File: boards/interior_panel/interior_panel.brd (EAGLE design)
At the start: 99.1 x 71.1 mm, 27 parts, among them IC1 LM2576, IC2 DS1307, J1 POWER_JACKPTH_BREAD, Q1 MOSFET-NCHANNELFQP30N06L, U1 ATMEGA328P, U2 EXT ENCLOSURE, U3 DISPLAY, Y1 16MHz, Y2 32.786kHz

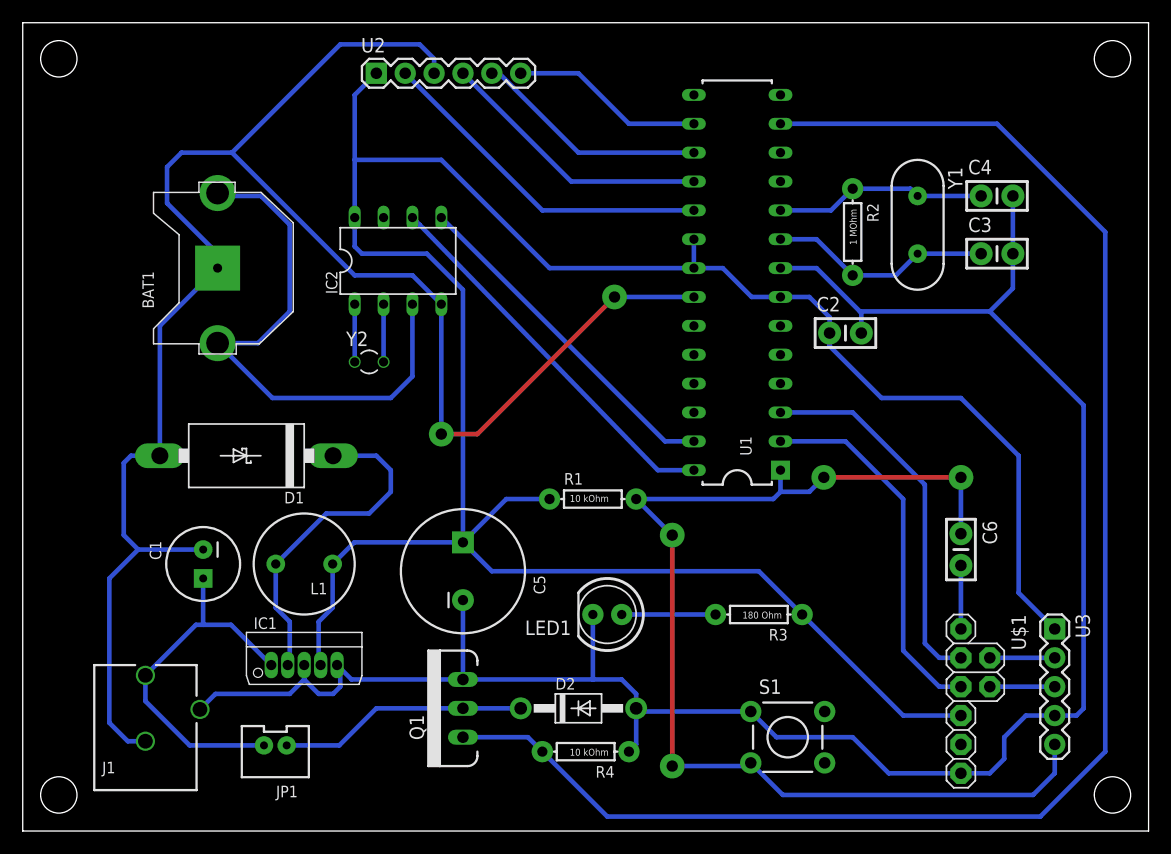
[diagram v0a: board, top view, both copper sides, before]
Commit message: Interior open command added
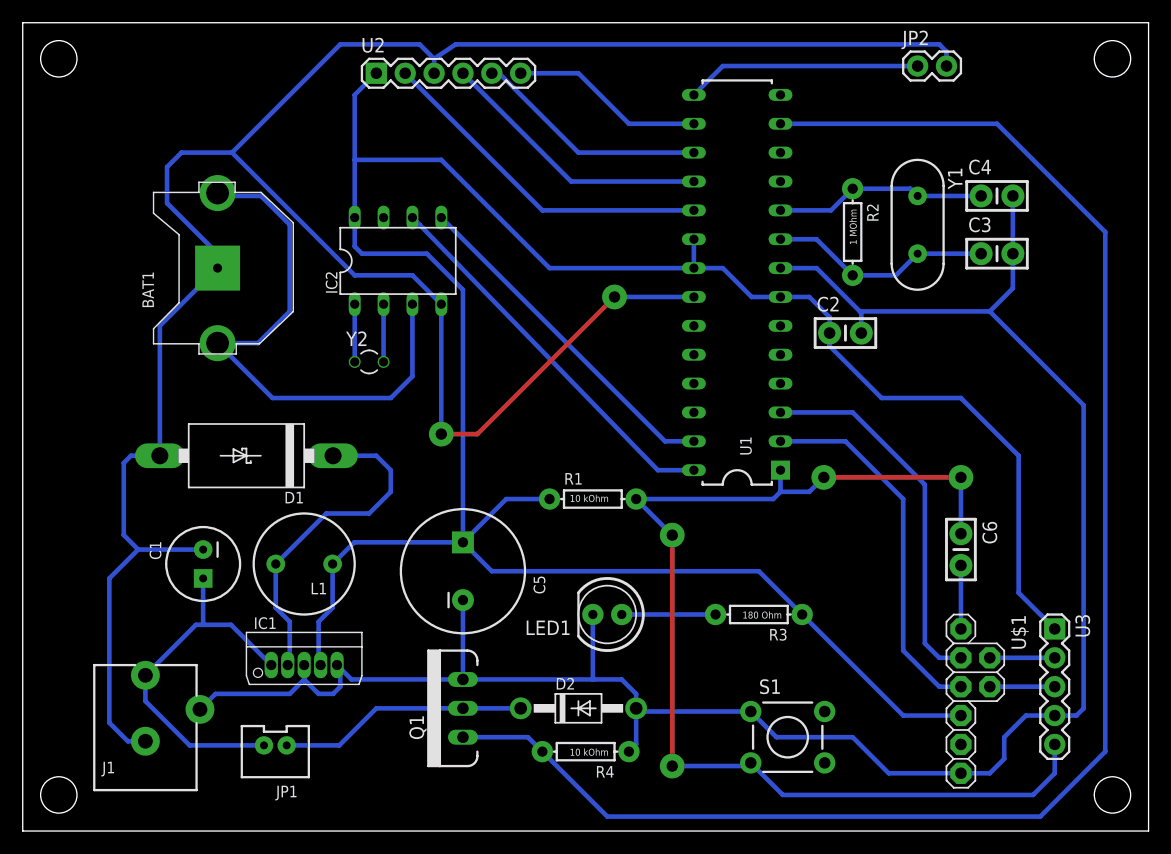
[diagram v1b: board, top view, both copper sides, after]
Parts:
- added JP2: M02PTH, nerdvellous-connectors:1X02
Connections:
- new net N$20: JP2.1, U1.15
- net GND: now also JP2.2
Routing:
- net GND: track 338.6 -> 385.6 mm
- net N$20: track 0.00 -> 20.7 mm
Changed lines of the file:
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@@
 <setting verticaltext="up"/>
 </settings>
-<grid distance="0.025" unitdist="inch" unit="inch" style="lines" multiple="1" display="no" altdistance="0.0125" altunitdist="inch" altunit="inch"/>
+<grid distance="0.025" unitdist="inch" unit="inch" style="lines" multiple="1" display="yes" altdistance="0.005" altunitdist="inch" altunit="inch"/>
 <layers>
-<layer number="1" name="Top" color="4" fill="1" visible="no" active="yes"/>
+<layer number="1" name="Top" color="4" fill="1" visible="yes" active="yes"/>
 <layer number="16" name="Bottom" color="1" fill="1" visible="yes" active="yes"/>
 <layer number="17" name="Pads" color="2" fill="1" visible="yes" active="yes"/>
 <layer number="18" name="Vias" color="2" fill="1" visible="yes" active="yes"/>
-<layer number="19" name="Unrouted" color="6" fill="1" visible="no" active="yes"/>
+<layer number="19" name="Unrouted" color="6" fill="1" visible="yes" active="yes"/>
 <layer number="20" name="Dimension" color="15" fill="1" visible="yes" active="yes"/>
-<layer number="21" name="tPlace" color="7" fill="1" visible="no" active="yes"/>
-<layer number="22" name="bPlace" color="7" fill="1" visible="no" active="yes"/>
-<layer number="23" name="tOrigins" color="15" fill="1" visible="no" active="yes"/>
-<layer number="24" name="bOrigins" color="15" fill="1" visible="no" active="yes"/>
+<layer number="21" name="tPlace" color="16" fill="1" visible="yes" active="yes"/>
+<layer number="22" name="bPlace" color="14" fill="1" visible="yes" active="yes"/>
+<layer number="23" name="tOrigins" color="15" fill="1" visible="yes" active="yes"/>
+<layer number="24" name="bOrigins" color="15" fill="1" visible="yes" active="yes"/>
 <layer number="25" name="tNames" color="7" fill="1" visible="no" active="yes"/>
 <layer number="26" name="bNames" color="7" fill="1" visible="no" active="yes"/>
@@
 <layer number="43" name="vRestrict" color="2" fill="10" visible="no" active="yes"/>
 <layer number="44" name="Drills" color="7" fill="1" visible="no" active="yes"/>
-<layer number="45" name="Holes" color="7" fill="1" visible="no" active="yes"/>
+<layer number="45" name="Holes" color="7" fill="1" visible="yes" active="yes"/>
 <layer number="46" name="Milling" color="3" fill="1" visible="no" active="yes"/>
 <layer number="47" name="Measures" color="7" fill="1" visible="no" active="yes"/>
@@
 <layer number="49" name="Reference" color="7" fill="1" visible="no" active="yes"/>
 <layer number="50" name="dxf" color="7" fill="1" visible="no" active="no"/>
-<layer number="51" name="tDocu" color="7" fill="1" visible="no" active="yes"/>
+<layer number="51" name="tDocu" color="6" fill="1" visible="yes" active="yes"/>
 <layer number="52" name="bDocu" color="7" fill="1" visible="no" active="yes"/>
 <layer number="53" name="tGND_GNDA" color="7" fill="9" visible="no" active="no"/>
@@
 <element name="Y1" library="nerdvellous-electromechanical" package="HC49US" value="16MHz" x="78.74" y="53.34" rot="R270"/>
 <element name="Y2" library="nerdvellous-electromechanical" package="TC26V" value="32.786kHz" x="30.48" y="41.275"/>
+<element name="JP2" library="nerdvellous-connectors" package="1X02" value="M02PTH" x="78.74" y="67.31"/>
 </elements>
 <signals>
@@
 <via x="36.83" y="34.925" extent="1-16" drill="1" diameter="2.1844"/>
 <wire x1="36.83" y1="34.925" x2="36.83" y2="46.355" width="0.4064" layer="16"/>
+<contactref element="JP2" pad="2"/>
+<wire x1="81.28" y1="67.31" x2="81.28" y2="68.58" width="0.4064" layer="16"/>
+<wire x1="81.28" y1="68.58" x2="80.645" y2="69.215" width="0.4064" layer="16"/>
+<wire x1="80.645" y1="69.215" x2="38.1" y2="69.215" width="0.4064" layer="16"/>
+<wire x1="38.1" y1="69.215" x2="36.195" y2="67.945" width="0.4064" layer="16"/>
 <wire x1="10.795" y1="7.9" x2="15.595" y2="10.7" width="0" layer="19" extent="1-1"/>
 </signal>
@@
 <wire x1="45.72" y1="54.61" x2="33.655" y2="66.675" width="0.4064" layer="16"/>
 </signal>
+<signal name="N$20">
+<contactref element="U1" pad="15"/>
+<contactref element="JP2" pad="1"/>
+<wire x1="78.74" y1="67.31" x2="61.595" y2="67.31" width="0.4064" layer="16"/>
+<wire x1="61.595" y1="67.31" x2="59.055" y2="64.77" width="0.4064" layer="16"/>
+</signal>
 </signals>
